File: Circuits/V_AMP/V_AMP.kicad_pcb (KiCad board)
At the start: 2 copper layers, 100 x 158 mm, 138 parts, among them P1 INPUT, P2 GAIN ON/OFF, P3 OUTPUT (0-5V), P4 POWER, U1 OPA277, U2 LM393, U3 OPA277

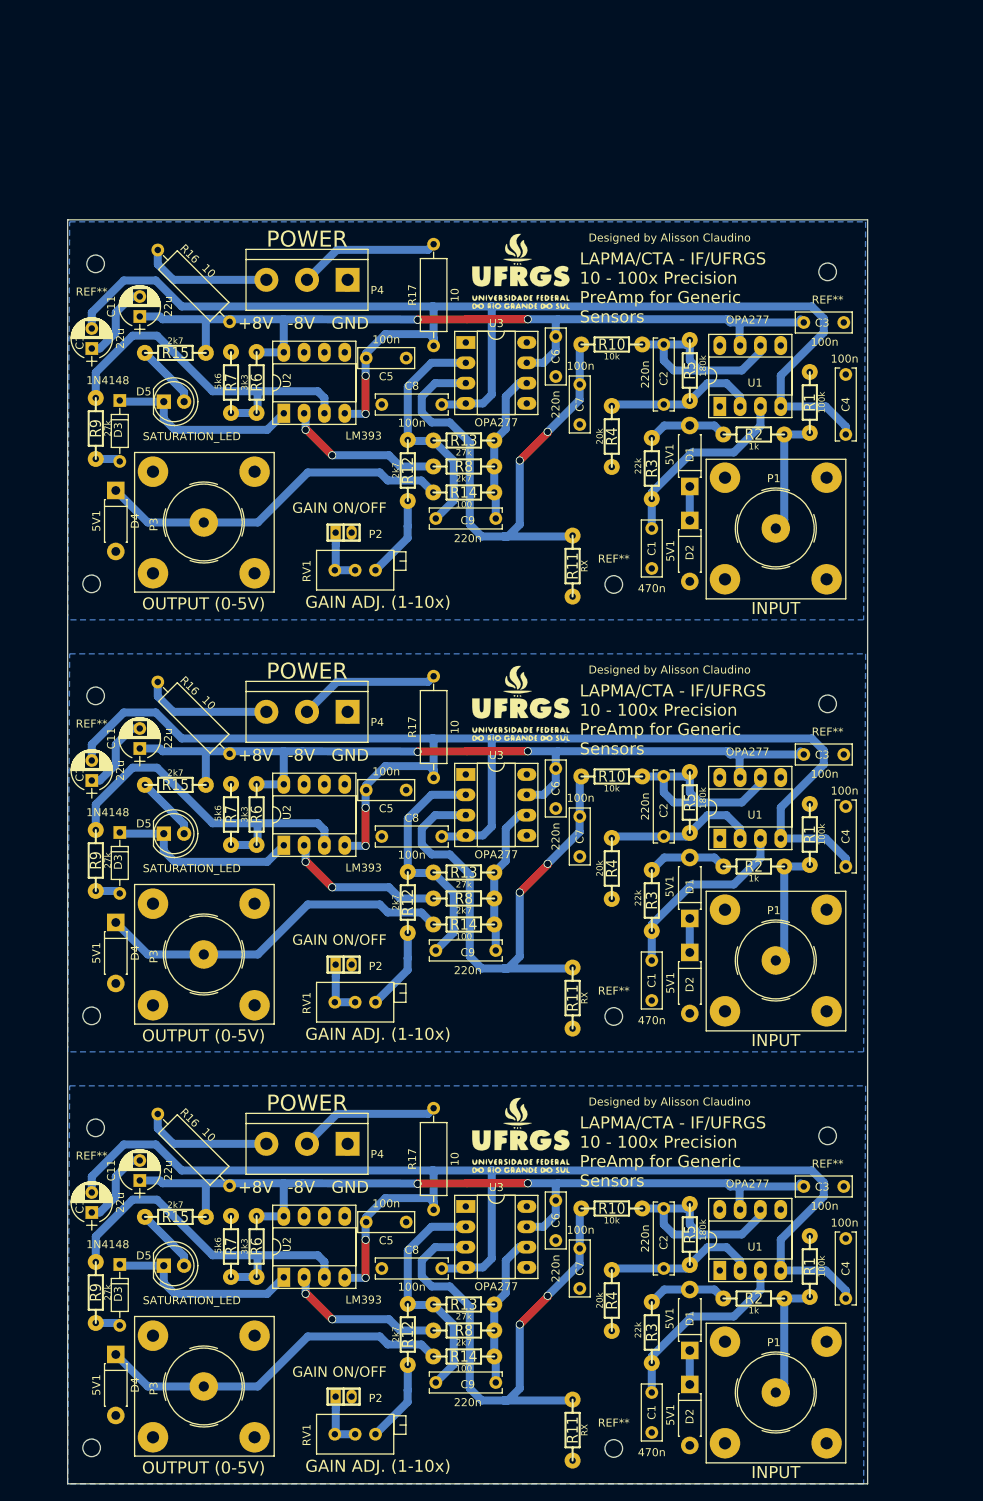
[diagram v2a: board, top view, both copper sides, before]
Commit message: ADD: V_AMP pcb design
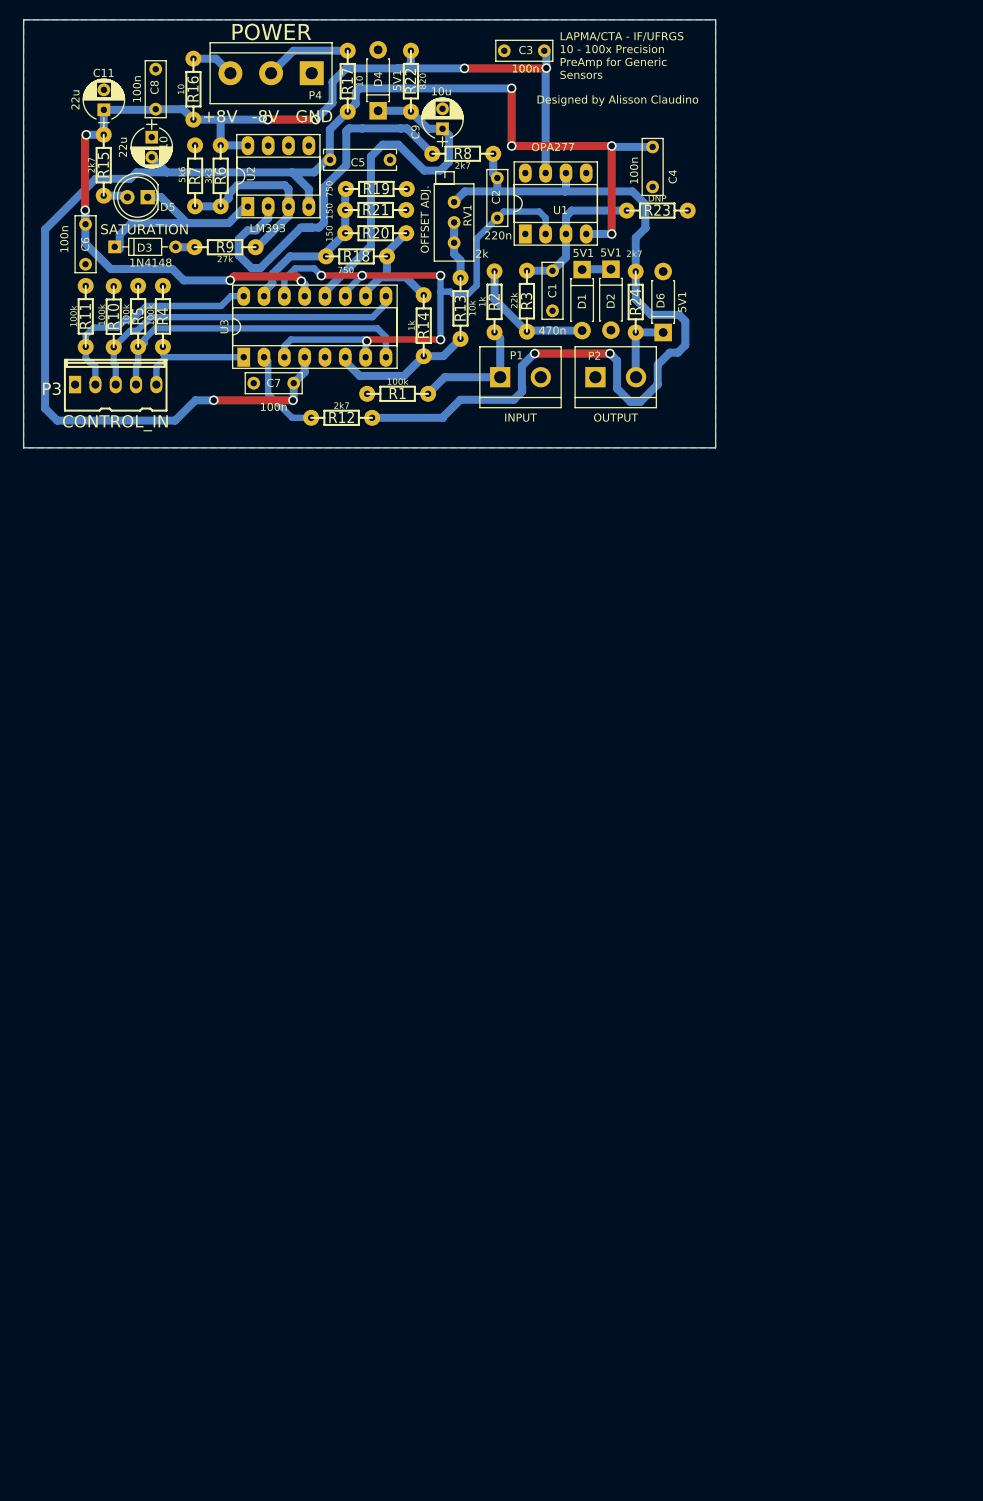
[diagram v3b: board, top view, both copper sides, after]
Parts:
- removed the C1 at (129.5, 93.1)
- removed the C1 at (129.5, 147.1)
- removed the C10 at (59.5, 70.6)
- removed the C10 at (59.5, 124.6)
- removed the C11 at (65.5, 66.6)
- removed the C11 at (65.5, 120.6)
- removed the C2 at (131.0, 70.1)
- removed the C2 at (131.0, 124.1)
- removed the C2 at (131.0, 178.1)
- removed the C3 at (153.5, 67.3)
- removed the C3 at (153.5, 121.3)
- removed the C3 at (153.5, 175.3)
- removed the C4 at (153.8, 73.8)
- removed the C4 at (153.8, 127.8)
- removed the C4 at (153.8, 181.8)
- removed the C5 at (98.8, 71.8)
- removed the C5 at (98.8, 125.8)
- removed the C5 at (98.8, 179.8)
- removed the C6 at (117.5, 74.1)
- removed the C6 at (117.5, 128.1)
- removed the C6 at (117.5, 182.1)
- removed the C7 at (120.5, 80.1)
- removed the C7 at (120.5, 134.1)
- removed the C7 at (120.5, 188.1)
- removed the C8 at (95.8, 77.6)
- removed the C8 at (95.8, 131.6)
- removed the C8 at (95.8, 185.6)
- removed the C9 at (102.5, 91.8)
- removed the C9 at (102.5, 145.8)
- removed the C9 at (102.5, 199.8)
- removed the D1 at (134.3, 87.8)
- removed the D1 at (134.3, 141.8)
- removed the D1 at (134.3, 195.8)
- removed the D2 at (134.3, 92.1)
- removed the D2 at (134.3, 146.1)
- removed the D3 at (63.0, 77.1)
- removed the D3 at (63.0, 131.1)
- removed the D3 at (63.0, 185.1)
- removed the D4 at (62.5, 88.3)
- removed the D4 at (62.5, 142.3)
- removed the D5 at (68.5, 77.2)
- removed the D5 at (68.5, 131.2)
- removed G*** (x3): LOGO, Symbols:ufrgs
- removed the P1 at (145.0, 93.1)
- removed the P1 at (145.0, 147.1)
- removed the P1 at (145.0, 201.1)
- removed the P2 at (91.0, 93.6)
- removed the P2 at (91.0, 147.6)
- removed the P2 at (91.0, 201.6)
- removed the P3 at (73.5, 92.3)
- removed the P3 at (73.5, 146.3)
- removed the P3 at (73.5, 200.3)
- removed the P4 at (91.5, 62.0)
- removed the P4 at (91.5, 116.0)
- removed the R1 at (149.3, 77.3)
- removed the R1 at (149.3, 131.3)
- removed the R1 at (149.3, 185.3)
- removed the R10 at (124.5, 70.1)
- removed the R10 at (124.5, 124.1)
- removed the R10 at (124.5, 178.1)
- removed the R11 at (119.6, 97.8)
- removed the R11 at (119.6, 151.8)
- removed the R12 at (99.0, 85.8)
- removed the R12 at (99.0, 139.8)
- removed the R12 at (99.0, 193.8)
- removed the R13 at (106.0, 82.1)
- removed the R13 at (106.0, 136.1)
- removed the R14 at (106.0, 88.6)
- removed the R14 at (106.0, 142.6)
- removed the R15 at (70.0, 71.1)
- removed the R15 at (70.0, 125.1)
- removed the R16 at (76.8, 67.2)
- removed the R16 at (76.8, 121.2)
- removed the R16 at (76.8, 175.2)
- removed the R17 at (102.2, 70.2)
- removed the R17 at (102.2, 124.2)
- removed the R17 at (102.2, 178.2)
- removed the R2 at (142.3, 81.3)
- removed the R2 at (142.3, 135.3)
- removed the R2 at (142.3, 189.3)
- removed the R3 at (129.5, 85.6)
- removed the R3 at (129.5, 139.6)
- removed the R4 at (124.5, 81.6)
- removed the R4 at (124.5, 135.6)
- removed the R4 at (124.5, 189.6)
- removed the R5 at (134.3, 73.3)
- removed the R5 at (134.3, 127.3)
- removed the R6 at (80.1, 74.8)
- removed the R6 at (80.1, 128.8)
- removed the R7 at (76.9, 74.8)
- removed the R7 at (76.9, 128.8)
- removed the R8 at (106.0, 85.3)
- removed the R8 at (106.0, 139.3)
- removed the R8 at (106.0, 193.3)
- removed the R9 at (60.0, 80.6)
- removed the R9 at (60.0, 134.6)
- removed the R9 at (60.0, 188.6)
- removed REF** (x12): MountingHole_2.2mm_M2, Mounting_Holes:MountingHole_2.2mm_M2
- removed the RV1 at (89.9, 98.3)
- removed the RV1 at (89.9, 152.3)
- removed the RV1 at (89.9, 206.3)
- removed the U1 at (138.0, 77.8)
- removed the U1 at (138.0, 131.8)
- removed the U1 at (138.0, 185.8)
- removed the U2 at (83.5, 78.7)
- removed the U2 at (83.5, 132.7)
- removed the U3 at (106.3, 69.8)
- removed the U3 at (106.3, 123.8)
- removed the U3 at (106.3, 177.8)
- added C2: 220n, Capacitors_THT:C_Rect_L7.0mm_W2.5mm_P5.00mm, F.Cu at (110.2, 49.3)
- added C3: 100n, Capacitors_THT:C_Rect_L7.0mm_W2.5mm_P5.00mm, F.Cu at (111.1, 33.4)
- added C4: 100n, Capacitors_THT:C_Rect_L7.0mm_W2.5mm_P5.00mm, F.Cu at (129.6, 50.4)
- added C5: 100n, Capacitors_THT:C_Rect_L9.0mm_W2.5mm_P7.50mm_MKT, F.Cu at (96.8, 47.0)
- added C6: 100n, Capacitors_THT:C_Rect_L7.0mm_W2.5mm_P5.00mm, F.Cu at (58.7, 60.0)
- added C7: 100n, Capacitors_THT:C_Rect_L7.0mm_W2.5mm_P5.00mm, F.Cu at (84.8, 74.9)
- added C8: 100n, Capacitors_THT:C_Rect_L7.0mm_W2.5mm_P5.00mm, F.Cu at (67.5, 35.7)
- added C9: 10u, Capacitors_THT:CP_Radial_D5.0mm_P2.50mm, F.Cu at (103.4, 43.1)
- added D1: 5V1, Diodes_THT:D_DO-41_SOD81_P7.62mm_Horizontal, F.Cu at (120.8, 60.7)
- added D3: 1N4148, Diodes_THT:D_DO-35_SOD27_P7.62mm_Horizontal, F.Cu at (62.4, 57.9)
- added D6: 5V1, Diodes_THT:D_DO-41_SOD81_P7.62mm_Horizontal, F.Cu at (130.9, 68.6)
- added P1: INPUT, Connect:bornier2, F.Cu at (113.1, 74.2)
- added P2: OUTPUT, Connect:bornier2, F.Cu at (125.0, 74.2)
- added P3: CONTROL_IN, w_conn_kk100:kk100_22-23-2051, F.Cu at (62.5, 75.2)
- added R1: 100k, w_pth_resistors:RC03, F.Cu at (97.8, 76.2)
- added R10: 100k, w_pth_resistors:RC03, F.Cu at (62.3, 66.6)
- added R12: 2k7, w_pth_resistors:RC03, F.Cu at (90.8, 79.2)
- added R16: 10, w_pth_resistors:RC03, F.Cu at (72.2, 38.2)
- added R17: 10, w_pth_resistors:RC03, F.Cu at (91.5, 37.2)
- added R18: 750, w_pth_resistors:RC03, F.Cu at (92.6, 59.1)
- added R19: 750, w_pth_resistors:RC03, F.Cu at (95.1, 50.6)
- added R2: 1k, w_pth_resistors:RC03, F.Cu at (109.9, 64.8)
- added R20: 150, w_pth_resistors:RC03, F.Cu at (95.0, 56.2)
- added R21: 150, w_pth_resistors:RC03, F.Cu at (95.0, 53.3)
- added R22: 820, w_pth_resistors:RC03, F.Cu at (99.4, 37.2)
- added R23: DNP, w_pth_resistors:RC03, F.Cu at (130.2, 53.3)
- added R24: 2k7, w_pth_resistors:RC03, F.Cu at (127.5, 64.8)
- added R4: 100k, w_pth_resistors:RC03, F.Cu at (68.4, 66.6)
- added R8: 2k7, w_pth_resistors:RC03, F.Cu at (105.9, 46.2)
- added R9: 27k, w_pth_resistors:RC03, F.Cu at (76.2, 57.9)
- added RV1: 2k, Potentiometers:Potentiometer_Trimmer_Bourns_3296X, F.Cu at (104.8, 57.4)
- added U1: OPA277, Housings_DIP:DIP-8_W7.62mm_Socket_LongPads, F.Cu at (113.7, 56.3)
- added U3: DG412xJ, Housings_DIP:DIP-16_W7.62mm_Socket_LongPads, F.Cu at (78.5, 71.7)
- D5: value SATURATION_LED -> SATURATION
- R11: value RX -> 100k
- R13: value 27k -> 10k
- R14: value 100 -> 1k
- R5: value 180k -> 100k
- moved D4 158.9 mm to (95.3, 40.9), turned to 90 degrees
- moved R11 151.9 mm to (58.8, 66.6), turned to 270 degrees
- moved C1 140.8 mm to (117.1, 60.9)
- moved D2 139.8 mm to (124.4, 60.7)
- moved C10 134.6 mm to (67.0, 44.2), turned to 270 degrees
- moved C11 133.9 mm to (61.0, 40.8)
- moved R6 133.9 mm to (75.6, 49.0)
- moved R7 133.9 mm to (72.4, 49.0)
- moved U2 133.9 mm to (79.0, 52.9)
- moved P4 133.9 mm to (87.0, 36.2)
- moved R5 133.9 mm to (65.3, 66.6)
- moved D5 133.6 mm to (66.5, 51.7), turned to 180 degrees
- moved R15 131.8 mm to (61.0, 47.7), turned to 270 degrees
- moved R3 129.9 mm to (113.9, 64.7), turned to 270 degrees
- moved R14 128.9 mm to (101.0, 67.7), turned to 270 degrees
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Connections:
- net Net-(C1-Pad1) renamed IN1
- D4 pad 1: Net-(D4-Pad1) -> Net-(C9-Pad1)
- R11 pad 2: Net-(C7-Pad2) -> b3
- R13 pad 1: Net-(C9-Pad1) -> Net-(R13-Pad1)
- R13 pad 2: OUT2 -> Net-(R13-Pad2)
- R14 pad 1: Net-(D4-Pad1) -> Net-(R14-Pad1)
- R14 pad 2: OUT2 -> Net-(R13-Pad1)
- R5 pad 1: OUT1 -> GND
- R5 pad 2: Net-(C2-Pad2) -> b1
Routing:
- net -8V: track 492.7 -> 176.6 mm
- net Net-(C7-Pad2): track 203.5 -> 0.00 mm, vias 6 -> 0
- net +8V: track 321.4 -> 137.0 mm, vias 6 -> 8
- net Net-(D4-Pad1): track 134.9 -> 0.00 mm
- net Net-(R6-Pad2): track 134.3 -> 23.3 mm
- net OUT2: track 57.7 -> 0.00 mm
- net IN1: track 71.9 -> 18.6 mm
- net Net-(D3-Pad1): track 72.4 -> 25.5 mm
- net Net-(C9-Pad1): track 90.4 -> 45.5 mm
- net Net-(P4-Pad2): track 56.0 -> 11.7 mm
- net Net-(P4-Pad3): track 49.8 -> 5.82 mm
- net b2: track 0.00 -> 42.8 mm
- net b1: track 0.00 -> 40.1 mm
- net GND: track 33.8 -> 1.10 mm
- net Net-(P1-Pad1): track 47.5 -> 16.5 mm
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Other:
- board size 100 x 158 mm -> 86.5 x 53.5 mm
- net class DIG_SIGNAL added: clearance 0.6, trace_width 0.8, via_dia 1.2, via_drill 0.8
- net class Default: via_dia 1 -> 1.2
- board text added: "OFFSET ADJ."
- board text removed: "GAIN ADJ. (1-10x)"

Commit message: EDIT: REORGANIZING FILES
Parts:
- added REF**: MountingHole_2.2mm_M2, Mounting_Holes:MountingHole_2.2mm_M2, F.Cu at (74.0, 76.0)
- added REF**: MountingHole_2.2mm_M2, Mounting_Holes:MountingHole_2.2mm_M2, F.Cu at (134.0, 43.0)
- added REF**: MountingHole_2.2mm_M2, Mounting_Holes:MountingHole_2.2mm_M2, F.Cu at (134.0, 79.5)
- added REF**: MountingHole_2.2mm_M2, Mounting_Holes:MountingHole_2.2mm_M2, F.Cu at (55.0, 33.5)
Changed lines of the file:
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@@
     (tracks 356)
     (zones 0)
-    (modules 49)
+    (modules 53)
     (nets 28)
   )
@@
     (aux_axis_origin 51 83)
     (grid_origin 33 81.5)
-    (visible_elements 7FFFE77F)
+    (visible_elements 7FFFEF7F)
     (pcbplotparams
-      (layerselection 0x00020_7ffffffe)
+      (layerselection 0x00000_fffffffe)
       (usegerberextensions false)
       (usegerberattributes false)
@@
       (padsonsilk true)
       (subtractmaskfromsilk false)
-      (outputformat 4)
+      (outputformat 1)
       (mirror false)
       (drillshape 0)
@@
     (add_net b2)
     (add_net b3)
+  )
+  (module Mounting_Holes:MountingHole_2.2mm_M2 (layer F.Cu)
+    (at 74 76)
+    (descr "Mounting Hole 2.2mm, no annular, M2")
+    (tags "mounting hole 2.2mm no annular m2")
+    (fp_text reference REF** (at 0 -3.2) (layer F.SilkS) hide
+      (effects (font (size 1 1) (thickness 0.15)))
+    )
+    (fp_text value MountingHole_2.2mm_M2 (at 0 3.2) (layer F.Fab) hide
+      (effects (font (size 1 1) (thickness 0.15)))
+    )
+    (fp_circle (center 0 0) (end 2.45 0) (layer F.CrtYd) (width 0.05))
+    (fp_circle (center 0 0) (end 2.2 0) (layer Cmts.User) (width 0.15))
+    (pad 1 np_thru_hole circle (at 0 0) (size 2.2 2.2) (drill 2.2) (layers *.Cu *.Mask))
+  )
+  (module Mounting_Holes:MountingHole_2.2mm_M2 (layer F.Cu)
+    (at 134 43)
+    (descr "Mounting Hole 2.2mm, no annular, M2")
+    (tags "mounting hole 2.2mm no annular m2")
+    (fp_text reference REF** (at 0.5 3.5) (layer F.SilkS) hide
+      (effects (font (size 1 1) (thickness 0.15)))
+    )
+    (fp_text value MountingHole_2.2mm_M2 (at 0 3.2) (layer F.Fab) hide
+      (effects (font (size 1 1) (thickness 0.15)))
+    )
+    (fp_circle (center 0 0) (end 2.45 0) (layer F.CrtYd) (width 0.05))
+    (fp_circle (center 0 0) (end 2.2 0) (layer Cmts.User) (width 0.15))
+    (pad 1 np_thru_hole circle (at 0 0) (size 2.2 2.2) (drill 2.2) (layers *.Cu *.Mask))
+  )
+  (module Mounting_Holes:MountingHole_2.2mm_M2 (layer F.Cu)
+    (at 134 79.5)
+    (descr "Mounting Hole 2.2mm, no annular, M2")
+    (tags "mounting hole 2.2mm no annular m2")
+    (fp_text reference REF** (at 0 -3.2) (layer F.SilkS) hide
+      (effects (font (size 1 1) (thickness 0.15)))
+    )
+    (fp_text value MountingHole_2.2mm_M2 (at 0 3.2) (layer F.Fab) hide
+      (effects (font (size 1 1) (thickness 0.15)))
+    )
+    (fp_circle (center 0 0) (end 2.2 0) (layer Cmts.User) (width 0.15))
+    (fp_circle (center 0 0) (end 2.45 0) (layer F.CrtYd) (width 0.05))
+    (pad 1 np_thru_hole circle (at 0 0) (size 2.2 2.2) (drill 2.2) (layers *.Cu *.Mask))
   )
   (module Housings_DIP:DIP-16_W7.62mm_Socket_LongPads (layer F.Cu)
@@
       (rotate (xyz 0 0 -90))
     )
+  )
+  (module Mounting_Holes:MountingHole_2.2mm_M2 (layer F.Cu)
+    (at 55 33.5)
+    (descr "Mounting Hole 2.2mm, no annular, M2")
+    (tags "mounting hole 2.2mm no annular m2")
+    (fp_text reference REF** (at 0 -3.2) (layer F.SilkS) hide
+      (effects (font (size 1 1) (thickness 0.15)))
+    )
+    (fp_text value MountingHole_2.2mm_M2 (at 0 3.2) (layer F.Fab) hide
+      (effects (font (size 1 1) (thickness 0.15)))
+    )
+    (fp_circle (center 0 0) (end 2.45 0) (layer F.CrtYd) (width 0.05))
+    (fp_circle (center 0 0) (end 2.2 0) (layer Cmts.User) (width 0.15))
+    (pad 1 np_thru_hole circle (at 0 0) (size 2.2 2.2) (drill 2.2) (layers *.Cu *.Mask))
   )
   (gr_line (start 137.5 29.5) (end 137.5 83) (layer Edge.Cuts) (width 0.15))
@@
   (segment (start 84.762 74.92) (end 84.762 76.966) (width 1) (layer B.Cu) (net 5) (status 10))
   (segment (start 84.762 76.966) (end 84.67 77.058) (width 1) (layer B.Cu) (net 5))
-  (via (at 74.764 77.058) (size 1.2) (drill 0.8) (layers F.Cu B.Cu) (net 5))
-  (segment (start 84.67 77.058) (end 74.764 77.058) (width 1) (layer F.Cu) (net 5))
-  (segment (start 69.938 79.598) (end 55.206 79.598) (width 1) (layer B.Cu) (net 5))
-  (segment (start 74.764 77.058) (end 72.478 77.058) (width 1) (layer B.Cu) (net 5))
-  (segment (start 72.478 77.058) (end 69.938 79.598) (width 1) (layer B.Cu) (net 5))
-  (segment (start 55.206 79.598) (end 53.682 78.074) (width 1) (layer B.Cu) (net 5))
-  (segment (start 53.682 55.702752) (end 60.012752 49.372) (width 1) (layer B.Cu) (net 5))
-  (segment (start 53.682 78.074) (end 53.682 55.702752) (width 1) (layer B.Cu) (net 5))
-  (segment (start 64.31 49.372) (end 65.11201 48.56999) (width 1) (layer B.Cu) (net 5))
-  (segment (start 65.11201 48.56999) (end 68.91199 48.56999) (width 1) (layer B.Cu) (net 5))
-  (segment (start 60.012752 49.372) (end 64.31 49.372) (width 1) (layer B.Cu) (net 5))
   (segment (start 124.468 45.226) (end 124.512 45.27) (width 1) (layer B.Cu) (net 5))
   (segment (start 124.63 45.388) (end 124.512 45.27) (width 1) (layer B.Cu) (net 5))
   (segment (start 129.628 45.388) (end 124.63 45.388) (width 1) (layer B.Cu) (net 5) (status 10))
+  (segment (start 65.11201 48.56999) (end 68.91199 48.56999) (width 1) (layer B.Cu) (net 5))
+  (segment (start 64.31 49.372) (end 65.11201 48.56999) (width 1) (layer B.Cu) (net 5))
+  (segment (start 60.012752 49.372) (end 64.31 49.372) (width 1) (layer B.Cu) (net 5))
+  (segment (start 53.682 78.074) (end 53.682 55.702752) (width 1) (layer B.Cu) (net 5))
+  (segment (start 53.682 55.702752) (end 60.012752 49.372) (width 1) (layer B.Cu) (net 5))
+  (segment (start 55.206 79.598) (end 55 79.392) (width 1) (layer B.Cu) (net 5))
+  (segment (start 55 79.392) (end 53.682 78.074) (width 1) (layer B.Cu) (net 5))
+  (segment (start 55.608 80) (end 55 79.392) (width 1) (layer B.Cu) (net 5))
+  (segment (start 84.67 77.058) (end 80 80) (width 1) (layer F.Cu) (net 5))
+  (via (at 80 80) (size 1.2) (drill 0.8) (layers F.Cu B.Cu) (net 5))
+  (segment (start 80 80) (end 55.608 80) (width 1) (layer B.Cu) (net 5))
   (segment (start 99.302 40.87) (end 99.412 40.98) (width 1) (layer B.Cu) (net 6) (status 30))
   (segment (start 95.312 40.87) (end 99.302 40.87) (width 1) (layer B.Cu) (net 6) (status 30))
@@
     (polygon
       (pts
-        (xy 137.5 29.5) (xy 137.5 83) (xy 51 83) (xy 51 29.5)
+        (xy 137.5 29.344486) (xy 137.5 82.844486) (xy 51.5 83) (xy 51.5 29.5)
       )
     )
